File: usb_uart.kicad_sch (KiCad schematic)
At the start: 23 parts, among them U60 FT232RL, U61 CP2102N-Axx-xQFN28, U62 CH340C

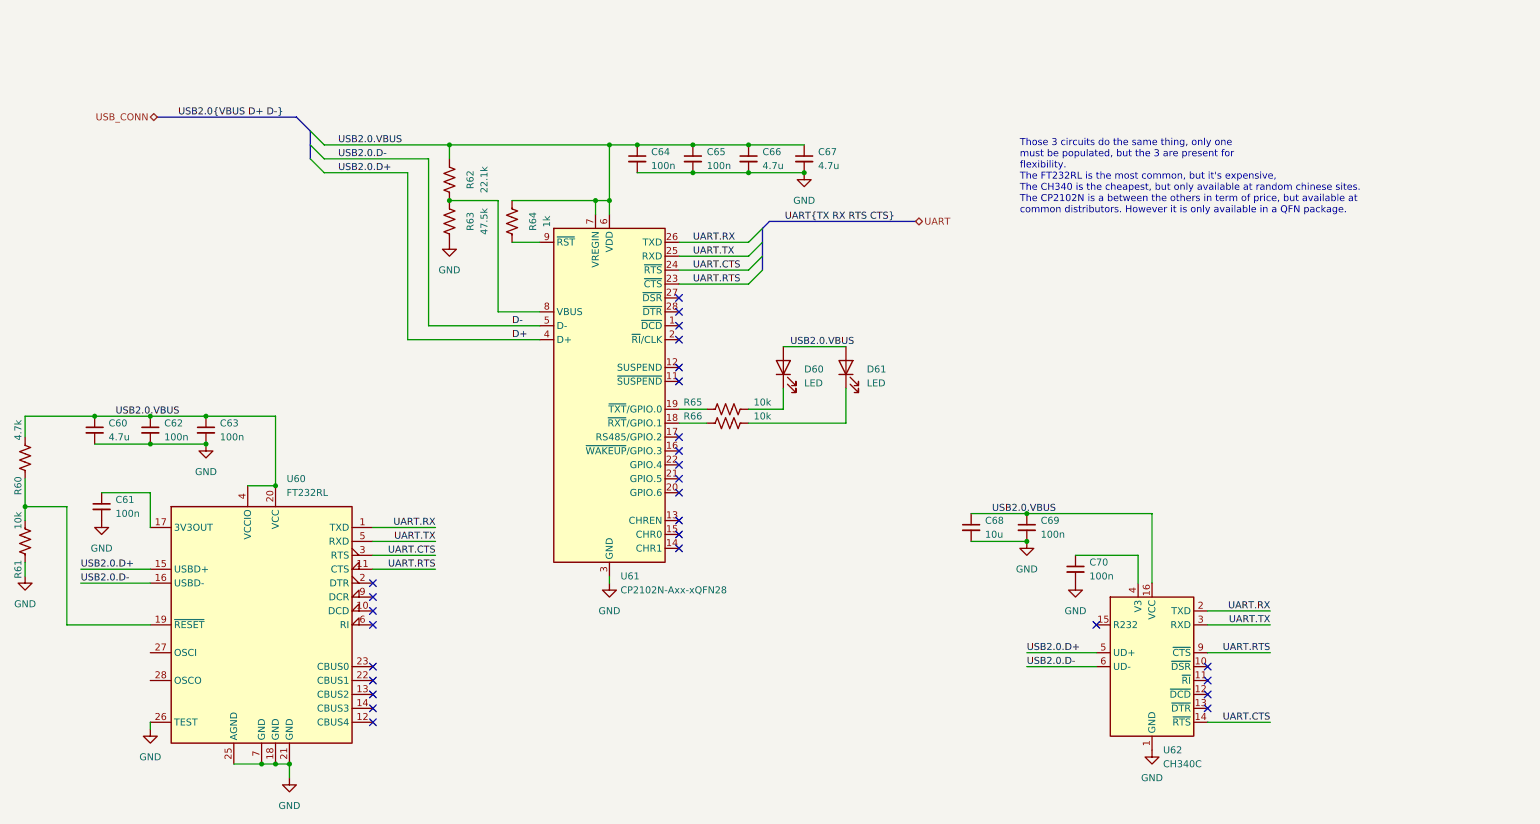
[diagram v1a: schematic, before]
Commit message: WIP PCB Routing + Add load voltage measure
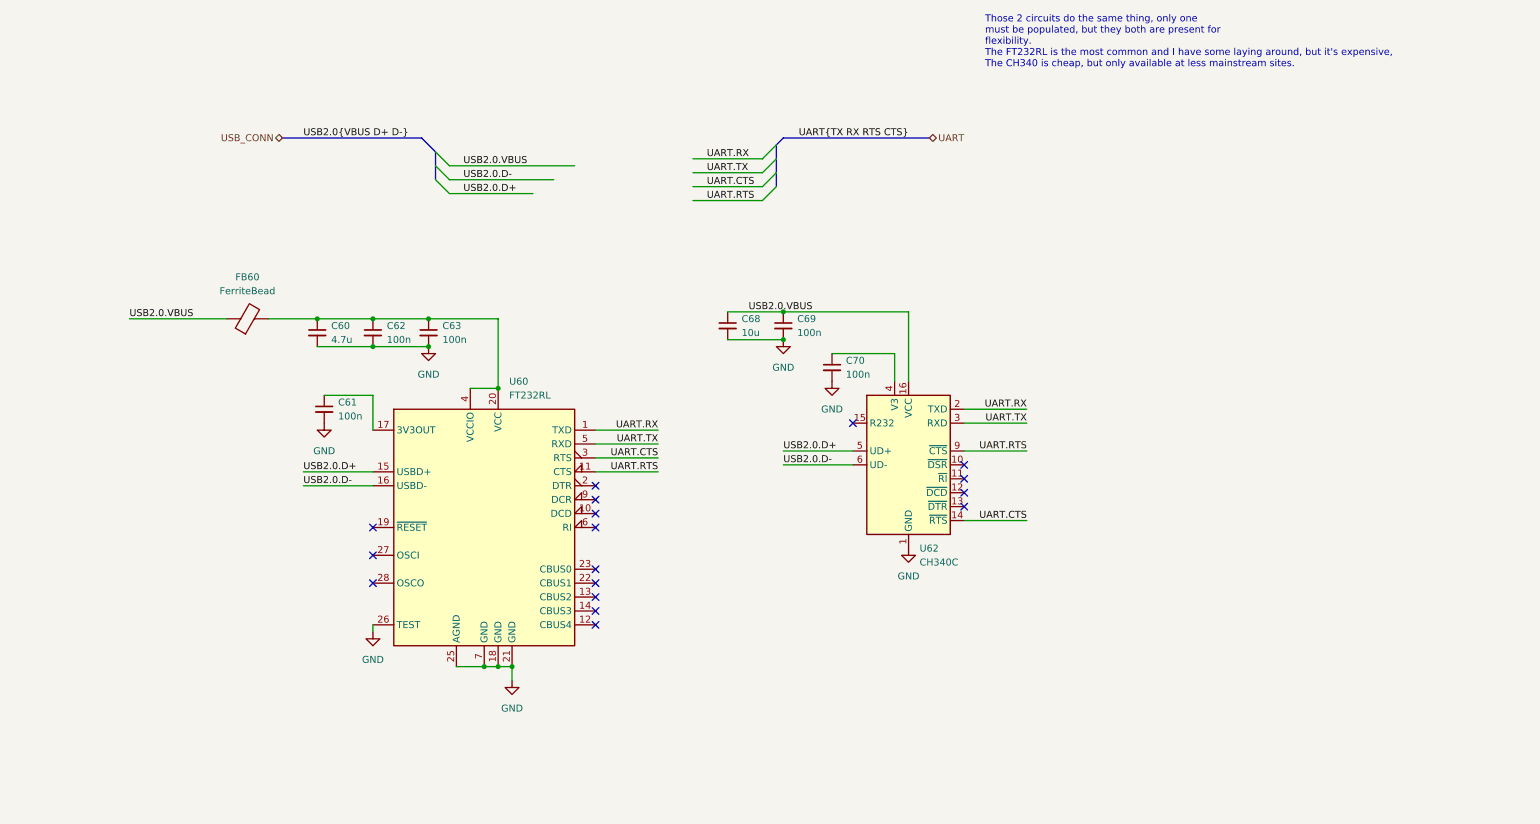
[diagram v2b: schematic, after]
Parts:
- removed C64, C65: 100n, Capacitor_SMD:C_0805_2012Metric, symbol Device:C_Small
- removed C66, C67: 4.7u, Capacitor_SMD:C_0805_2012Metric, symbol Device:C_Small
- removed D60, D61: LED, LED_SMD:LED_0805_2012Metric, symbol Device:LED
- removed R60: 4.7k, Resistor_SMD:R_0805_2012Metric, symbol Device:R_US
- removed R61, R65, R66: 10k, Resistor_SMD:R_0805_2012Metric, symbol Device:R_US
- removed R62: 22.1k, Resistor_SMD:R_0805_2012Metric, symbol Device:R_US
- removed R63: 47.5k, Resistor_SMD:R_0805_2012Metric, symbol Device:R_US
- removed R64: 1k, Resistor_SMD:R_0805_2012Metric, symbol Device:R_US
- removed U61: CP2102N-Axx-xQFN28, Package_DFN_QFN:QFN-28-1EP_5x5mm_P0.5mm_EP3.35x3.35mm, symbol Interface_USB:CP2102N-Axx-xQFN28
- added FB60: FerriteBead, Inductor_SMD:L_0805_2012Metric, symbol Device:FerriteBead
- C61, C62, C63, C69, C70: footprint Capacitor_SMD:C_0805_2012Metric -> Capacitor_SMD:C_0402_1005Metric
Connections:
- net USB2.0.VBUS: now also FB60.1; no longer C60.1, C62.1, C63.1, U60.20 (VCC), U60.4 (VCCIO)
- net D+ renamed USB2.0.D+
- net D- renamed USB2.0.D-
- new net: C60.1, C62.1, C63.1, FB60.2, U60.20 (VCC), U60.4 (VCCIO)
- no-connect marks 28 -> 17
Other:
- note added: "Those 2 circuits do the same thing, only one must be populated, but they both are present for flexibility. The FT232RL is the most common and I have some laying around, but it's expensive, The CH340 is cheap, but only available at less mainstream sites."
- note removed: "Those 3 circuits do the same thing, only one must be populated, but the 3 are present for flexibility. The FT232RL is the most common, but it's expensive, The CH340 is the cheapest, but only available at random chinese sites. The CP2102N is a between the others in term of price, but available at common distributors. However it is only available in a QFN package."
- moved on the sheet: C60, C61, C62, C63, C68, C69, C70, U60, U62

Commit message: WIP routing
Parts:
- C401: renamed from C60; value 4.7u -> (none); footprint Capacitor_SMD:C_0805_2012Metric -> (none)
- C402: renamed from C61; value 100n -> (none); footprint Capacitor_SMD:C_0402_1005Metric -> (none)
- C403: renamed from C62; value 100n -> (none); footprint Capacitor_SMD:C_0402_1005Metric -> (none)
- C404: renamed from C63; value 100n -> (none); footprint Capacitor_SMD:C_0402_1005Metric -> (none)
- C405: renamed from C68; value 10u -> (none); footprint Capacitor_SMD:C_0805_2012Metric -> (none)
- C406: renamed from C69; value 100n -> (none); footprint Capacitor_SMD:C_0402_1005Metric -> (none)
- C407: renamed from C70; value 100n -> (none); footprint Capacitor_SMD:C_0402_1005Metric -> (none)
- FB401: renamed from FB60; value FerriteBead -> (none); footprint Inductor_SMD:L_0805_2012Metric -> (none)
- U401: renamed from U60; value FT232RL -> (none); footprint Package_SO:SSOP-28_5.3x10.2mm_P0.65mm -> (none)
- U402: renamed from U62; value CH340C -> (none); footprint Package_SO:SOIC-16_3.9x9.9mm_P1.27mm -> (none)

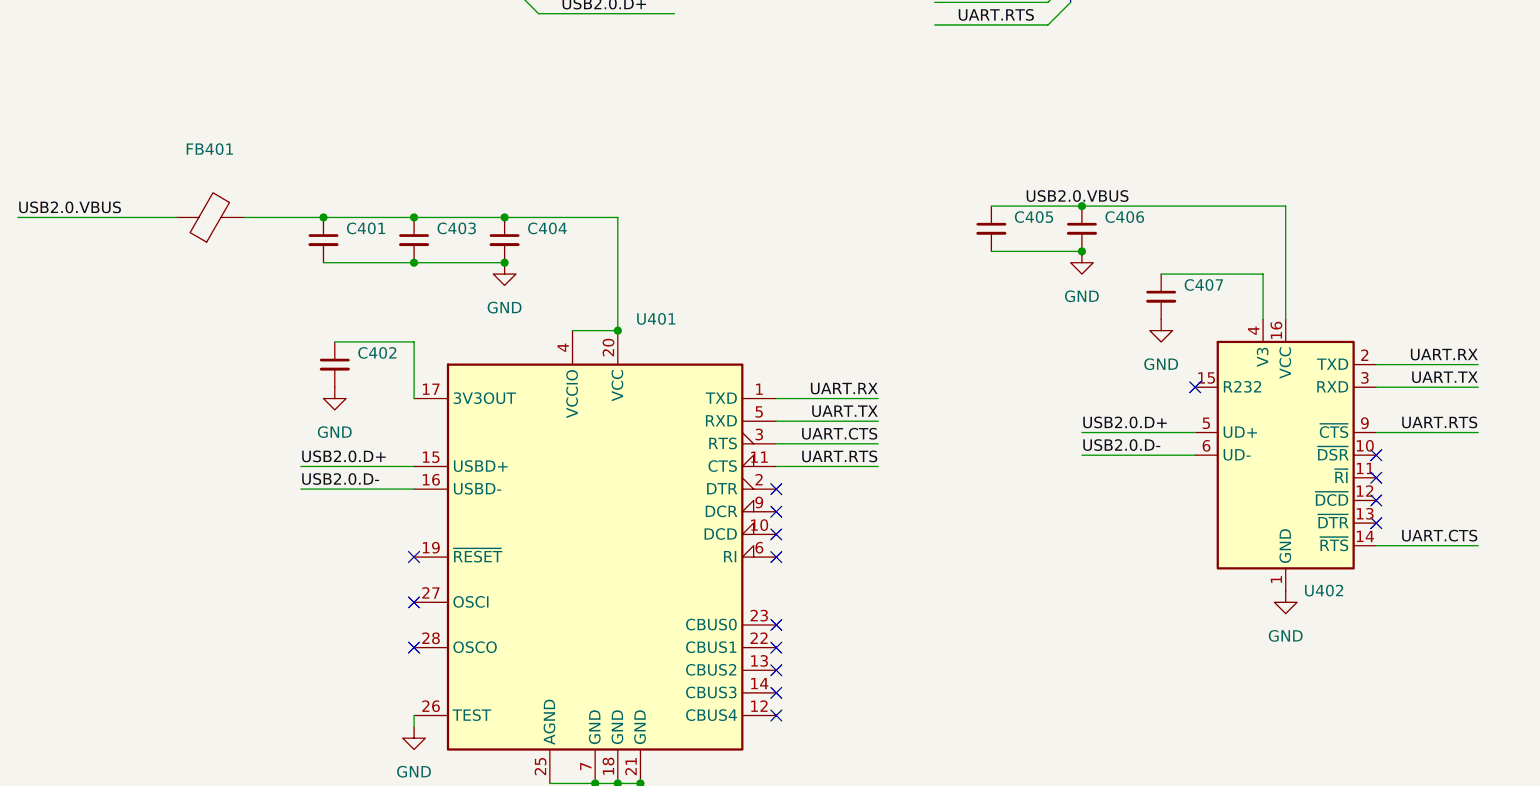
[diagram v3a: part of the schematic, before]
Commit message: Fix and tune differential pair and zones
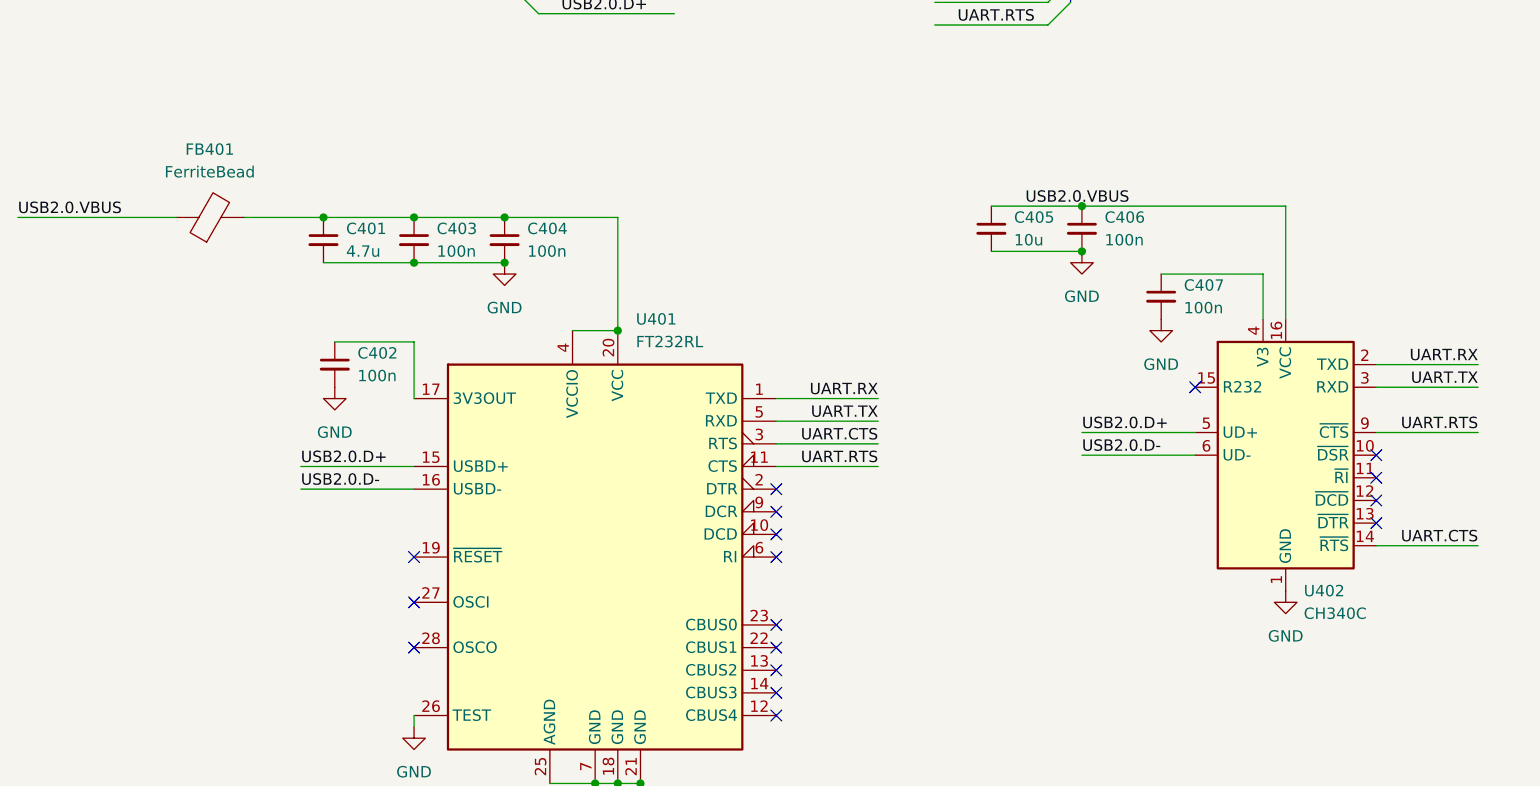
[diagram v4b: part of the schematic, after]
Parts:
- C401: value (none) -> 4.7u; footprint (none) -> Capacitor_SMD:C_0805_2012Metric
- C402, C403, C404, C406, C407: value (none) -> 100n; footprint (none) -> Capacitor_SMD:C_0402_1005Metric
- C405: value (none) -> 10u; footprint (none) -> Capacitor_SMD:C_0805_2012Metric
- FB401: value (none) -> FerriteBead; footprint (none) -> Inductor_SMD:L_0805_2012Metric
- U401: value (none) -> FT232RL; footprint (none) -> Package_SO:SSOP-28_5.3x10.2mm_P0.65mm
- U402: value (none) -> CH340C; footprint (none) -> Package_SO:SOIC-16_3.9x9.9mm_P1.27mm
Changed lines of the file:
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@@
       (effects (font (size 1.27 1.27)) (justify left))
     )
-    (property "Value" "" (id 1) (at 76.2 88.9062 0)
-      (effects (font (size 1.27 1.27)) (justify left))
-    )
-    (property "Footprint" "" (id 2) (at 73.66 87.63 0)
+    (property "Value" "100n" (id 1) (at 76.2 88.9062 0)
+      (effects (font (size 1.27 1.27)) (justify left))
+    )
+    (property "Footprint" "Capacitor_SMD:C_0402_1005Metric" (id 2) (at 73.66 87.63 0)
       (effects (font (size 1.27 1.27)) hide)
     )
@@
       (effects (font (size 1.27 1.27)) (justify left))
     )
-    (property "Value" "" (id 1) (at 107.4294 85.09 0)
-      (effects (font (size 1.27 1.27)) (justify left))
-    )
-    (property "Footprint" "" (id 2) (at 130.81 132.08 0)
+    (property "Value" "FT232RL" (id 1) (at 107.4294 85.09 0)
+      (effects (font (size 1.27 1.27)) (justify left))
+    )
+    (property "Footprint" "Package_SO:SSOP-28_5.3x10.2mm_P0.65mm" (id 2) (at 130.81 132.08 0)
       (effects (font (size 1.27 1.27)) hide)
     )
@@
       (effects (font (size 1.27 1.27)) (justify left))
     )
-    (property "Value" "" (id 1) (at 182.3594 115.57 0)
-      (effects (font (size 1.27 1.27)) (justify left))
-    )
-    (property "Footprint" "" (id 2) (at 181.61 111.76 0)
+    (property "Value" "CH340C" (id 1) (at 182.3594 115.57 0)
+      (effects (font (size 1.27 1.27)) (justify left))
+    )
+    (property "Footprint" "Package_SO:SOIC-16_3.9x9.9mm_P1.27mm" (id 2) (at 181.61 111.76 0)
       (effects (font (size 1.27 1.27)) (justify left) hide)
     )
@@
       (effects (font (size 1.27 1.27)) (justify left))
     )
-    (property "Value" "" (id 1) (at 85.09 74.9362 0)
-      (effects (font (size 1.27 1.27)) (justify left))
-    )
-    (property "Footprint" "" (id 2) (at 82.55 73.66 0)
+    (property "Value" "100n" (id 1) (at 85.09 74.9362 0)
+      (effects (font (size 1.27 1.27)) (justify left))
+    )
+    (property "Footprint" "Capacitor_SMD:C_0402_1005Metric" (id 2) (at 82.55 73.66 0)
       (effects (font (size 1.27 1.27)) hide)
     )
@@
       (effects (font (size 1.27 1.27)) (justify left))
     )
-    (property "Value" "" (id 1) (at 168.91 81.2862 0)
-      (effects (font (size 1.27 1.27)) (justify left))
-    )
-    (property "Footprint" "" (id 2) (at 166.37 80.01 0)
+    (property "Value" "100n" (id 1) (at 168.91 81.2862 0)
+      (effects (font (size 1.27 1.27)) (justify left))
+    )
+    (property "Footprint" "Capacitor_SMD:C_0402_1005Metric" (id 2) (at 166.37 80.01 0)
       (effects (font (size 1.27 1.27)) hide)
     )
@@
       (effects (font (size 1.27 1.27)) (justify left))
     )
-    (property "Value" "" (id 1) (at 149.86 73.6662 0)
-      (effects (font (size 1.27 1.27)) (justify left))
-    )
-    (property "Footprint" "" (id 2) (at 147.32 72.39 0)
+    (property "Value" "10u" (id 1) (at 149.86 73.6662 0)
+      (effects (font (size 1.27 1.27)) (justify left))
+    )
+    (property "Footprint" "Capacitor_SMD:C_0805_2012Metric" (id 2) (at 147.32 72.39 0)
       (effects (font (size 1.27 1.27)) hide)
     )
@@
       (effects (font (size 1.27 1.27)) (justify left))
     )
-    (property "Value" "" (id 1) (at 160.02 73.6662 0)
-      (effects (font (size 1.27 1.27)) (justify left))
-    )
-    (property "Footprint" "" (id 2) (at 157.48 72.39 0)
+    (property "Value" "100n" (id 1) (at 160.02 73.6662 0)
+      (effects (font (size 1.27 1.27)) (justify left))
+    )
+    (property "Footprint" "Capacitor_SMD:C_0402_1005Metric" (id 2) (at 157.48 72.39 0)
       (effects (font (size 1.27 1.27)) hide)
     )
@@
       (effects (font (size 1.27 1.27)) (justify left))
     )
-    (property "Value" "" (id 1) (at 95.25 74.9362 0)
-      (effects (font (size 1.27 1.27)) (justify left))
-    )
-    (property "Footprint" "" (id 2) (at 92.71 73.66 0)
+    (property "Value" "100n" (id 1) (at 95.25 74.9362 0)
+      (effects (font (size 1.27 1.27)) (justify left))
+    )
+    (property "Footprint" "Capacitor_SMD:C_0402_1005Metric" (id 2) (at 92.71 73.66 0)
       (effects (font (size 1.27 1.27)) hide)
     )
@@
       (effects (font (size 1.27 1.27)) (justify left))
     )
-    (property "Value" "" (id 1) (at 74.93 74.9362 0)
-      (effects (font (size 1.27 1.27)) (justify left))
-    )
-    (property "Footprint" "" (id 2) (at 72.39 73.66 0)
+    (property "Value" "4.7u" (id 1) (at 74.93 74.9362 0)
+      (effects (font (size 1.27 1.27)) (justify left))
+    )
+    (property "Footprint" "Capacitor_SMD:C_0805_2012Metric" (id 2) (at 72.39 73.66 0)
       (effects (font (size 1.27 1.27)) hide)
     )
@@
     (in_bom yes) (on_board yes) (fields_autoplaced)
     (property "Reference" "FB401" (id 0) (at 59.6392 63.5 90))
-    (property "Value" "" (id 1) (at 59.6392 66.04 90))
-    (property "Footprint" "" (id 2) (at 59.69 72.898 90)
-      (effects (font (size 1.27 1.27)) hide)
-    )
+    (property "Value" "FerriteBead" (id 1) (at 59.6392 66.04 90))
+    (property "Footprint" "Inductor_SMD:L_0805_2012Metric" (id 2) (at 59.69 72.898 90)
+      (effects (font (size 1.27 1.27)) hide)
+    )
